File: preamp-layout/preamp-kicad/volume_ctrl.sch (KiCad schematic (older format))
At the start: 63 parts, among them J65 Conn_01x02_Male, J66 Conn_01x02_Male, J67 Conn_01x03_Female, J68 Conn_01x03_Female, J69 Conn_01x03_Male, J70 Conn_01x03_Male, J71 Conn_01x03_Male, U12 MCP4902, U13 MCP4902, U14 TL072, U15 TL072, U16 THAT2181, U17 THAT2181, U18 TL072, U19 THAT2181, U20 THAT2181, U21 TL072

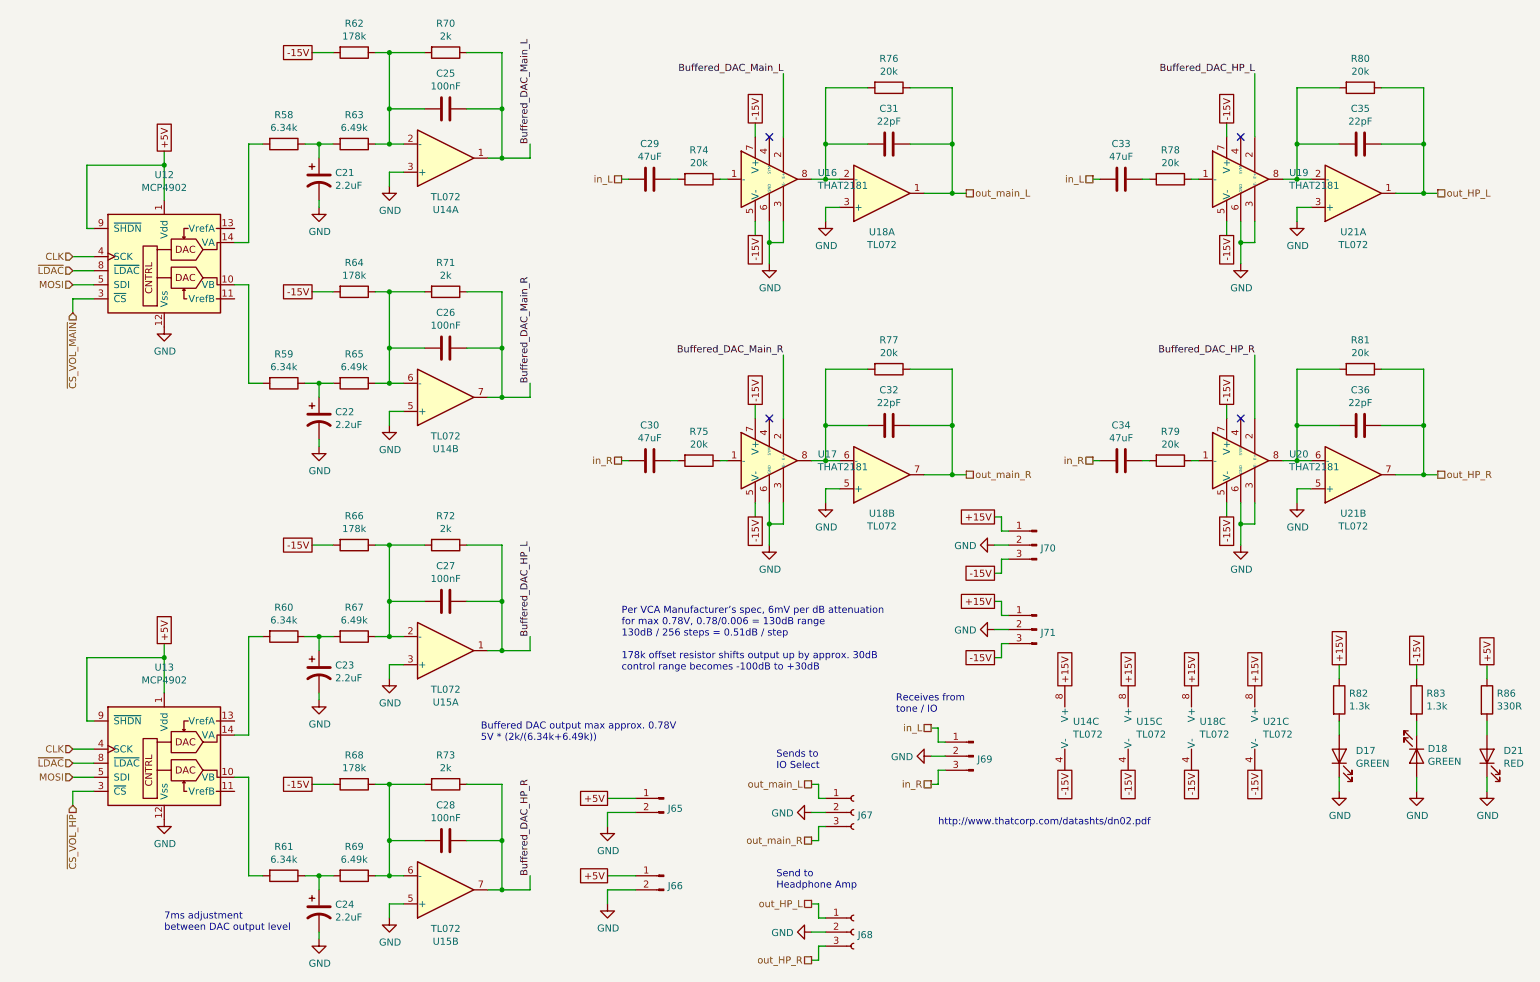
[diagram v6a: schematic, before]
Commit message: Initial Review
Reviewing schematic, comparing to references and filling in BOM to match schematics. Updating footprints in the process as well.
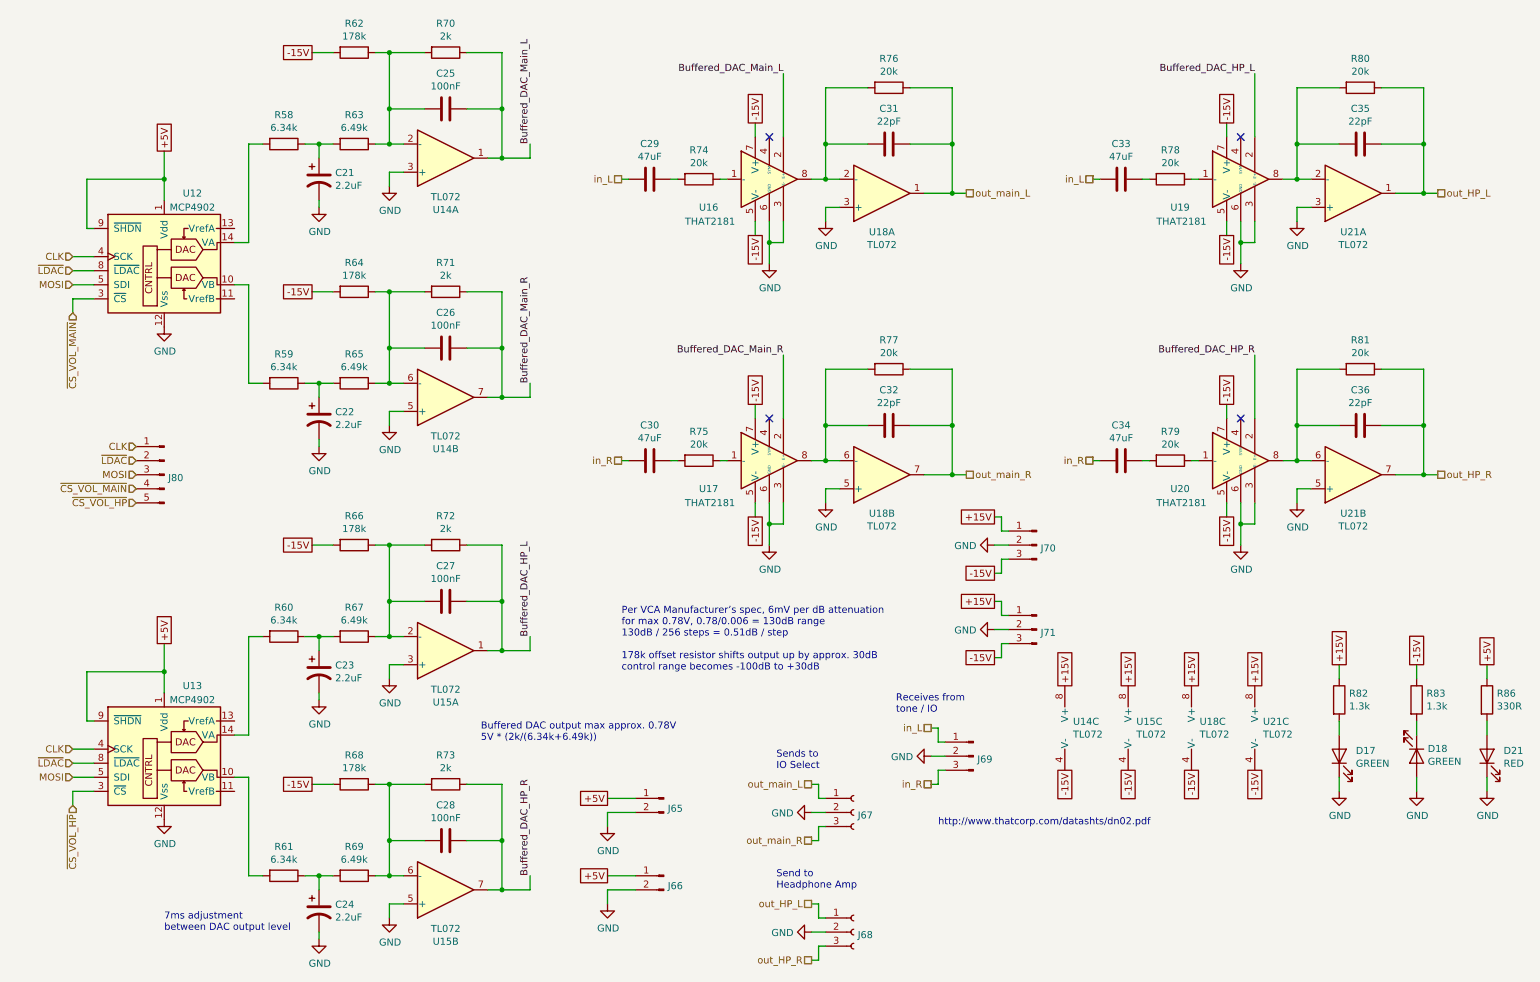
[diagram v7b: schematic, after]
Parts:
- added J80: Conn_01x05_Male, symbol Connector:Conn_01x05_Male
- C25, C26, C27, C28: footprint (none) -> Capacitor_SMD:C_0805_2012Metric_Pad1.15x1.40mm_HandSolder
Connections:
- net CLK: now also J80.1 (Pin_1)
- net MOSI: now also J80.3 (Pin_3)
- net ~CS_VOL_HP: now also J80.5 (Pin_5)
- net ~CS_VOL_MAIN: now also J80.4 (Pin_4)
- net ~LDAC: now also J80.2 (Pin_2)
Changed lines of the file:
@@
 $Descr A4 11693 8268
 encoding utf-8
-Sheet 11 12
+Sheet 12 12
 Title ""
 Date "2020-01-23"
@@
 F 0 "C25" V 3248 1400 50  0000 C CNN
 F 1 "100nF" V 3339 1400 50  0000 C CNN
-F 2 "" H 3538 1250 50  0001 C CNN
+F 2 "Capacitor_SMD:C_0805_2012Metric_Pad1.15x1.40mm_HandSolder" H 3538 1250 50  0001 C CNN
 F 3 "~" H 3500 1400 50  0001 C CNN
 	1    3500 1400
@@
 U 1 1 6017A289
 P 1500 2450
-F 0 "U12" H 1500 3031 50  0000 C CNN
-F 1 "MCP4902" H 1500 2940 50  0000 C CNN
+F 0 "U12" H 1700 2900 50  0000 C CNN
+F 1 "MCP4902" H 1700 2800 50  0000 C CNN
 F 2 "" H 2300 2150 50  0001 C CNN
 F 3 "http://ww1.microchip.com/downloads/en/DeviceDoc/22250A.pdf" H 2300 2150 50  0001 C CNN
@@
 U 1 1 6017683C
 P 5800 1900
-F 0 "U16" H 6144 1946 50  0000 L CNN
-F 1 "THAT2181" H 6144 1855 50  0000 L CNN
+F 0 "U16" H 5300 1700 50  0000 L CNN
+F 1 "THAT2181" H 5200 1600 50  0000 L CNN
 F 2 "" H 5800 1900 50  0001 C CNN
 F 3 "http://www.thatcorp.com/datashts/THAT_2181-Series_Datasheet.pdf" H 5800 1900 50  0001 C CNN
@@
 F 0 "C26" V 3248 3100 50  0000 C CNN
 F 1 "100nF" V 3339 3100 50  0000 C CNN
-F 2 "" H 3538 2950 50  0001 C CNN
+F 2 "Capacitor_SMD:C_0805_2012Metric_Pad1.15x1.40mm_HandSolder" H 3538 2950 50  0001 C CNN
 F 3 "~" H 3500 3100 50  0001 C CNN
 	1    3500 3100
@@
 U 1 1 602F6E92
 P 5800 3900
-F 0 "U17" H 6144 3946 50  0000 L CNN
-F 1 "THAT2181" H 6144 3855 50  0000 L CNN
+F 0 "U17" H 5300 3700 50  0000 L CNN
+F 1 "THAT2181" H 5200 3600 50  0000 L CNN
 F 2 "" H 5800 3900 50  0001 C CNN
 F 3 "http://www.thatcorp.com/datashts/THAT_2181-Series_Datasheet.pdf" H 5800 3900 50  0001 C CNN
@@
 F 0 "C27" V 3248 4900 50  0000 C CNN
 F 1 "100nF" V 3339 4900 50  0000 C CNN
-F 2 "" H 3538 4750 50  0001 C CNN
+F 2 "Capacitor_SMD:C_0805_2012Metric_Pad1.15x1.40mm_HandSolder" H 3538 4750 50  0001 C CNN
 F 3 "~" H 3500 4900 50  0001 C CNN
 	1    3500 4900
@@
 U 1 1 6033B91D
 P 1500 5950
-F 0 "U13" H 1500 6531 50  0000 C CNN
-F 1 "MCP4902" H 1500 6440 50  0000 C CNN
+F 0 "U13" H 1700 6400 50  0000 C CNN
+F 1 "MCP4902" H 1700 6300 50  0000 C CNN
 F 2 "" H 2300 5650 50  0001 C CNN
 F 3 "http://ww1.microchip.com/downloads/en/DeviceDoc/22250A.pdf" H 2300 5650 50  0001 C CNN
@@
 U 1 1 6033B96D
 P 9150 1900
-F 0 "U19" H 9494 1946 50  0000 L CNN
-F 1 "THAT2181" H 9494 1855 50  0000 L CNN
+F 0 "U19" H 8650 1700 50  0000 L CNN
+F 1 "THAT2181" H 8550 1600 50  0000 L CNN
 F 2 "" H 9150 1900 50  0001 C CNN
 F 3 "http://www.thatcorp.com/datashts/THAT_2181-Series_Datasheet.pdf" H 9150 1900 50  0001 C CNN
@@
 F 0 "C28" V 3248 6600 50  0000 C CNN
 F 1 "100nF" V 3339 6600 50  0000 C CNN
-F 2 "" H 3538 6450 50  0001 C CNN
+F 2 "Capacitor_SMD:C_0805_2012Metric_Pad1.15x1.40mm_HandSolder" H 3538 6450 50  0001 C CNN
 F 3 "~" H 3500 6600 50  0001 C CNN
 	1    3500 6600
@@
 U 1 1 6033BA78
 P 9150 3900
-F 0 "U20" H 9494 3946 50  0000 L CNN
-F 1 "THAT2181" H 9494 3855 50  0000 L CNN
+F 0 "U20" H 8650 3700 50  0000 L CNN
+F 1 "THAT2181" H 8550 3600 50  0000 L CNN
 F 2 "" H 9150 3900 50  0001 C CNN
 F 3 "http://www.thatcorp.com/datashts/THAT_2181-Series_Datasheet.pdf" H 9150 3900 50  0001 C CNN
@@
 	850  2550 1000 2550
 Wire Wire Line
-	1500 1700 1500 1800
-Wire Wire Line
 	1000 2250 950  2250
 Wire Wire Line
-	950  2250 950  1800
-Connection ~ 1500 1800
-Wire Wire Line
-	1500 1800 1500 2050
+	950  2250 950  1900
 Wire Wire Line
 	1000 5750 950  5750
 Wire Wire Line
-	950  5750 950  5300
-Wire Wire Line
-	950  5300 1500 5300
+	950  5750 950  5400
+Wire Wire Line
+	950  5400 1500 5400
 Text GLabel 1500 5200 1    50   UnSpc ~ 0
 +5V
 Wire Wire Line
-	1500 5200 1500 5300
-Wire Wire Line
-	1500 5300 1500 5550
-Connection ~ 1500 5300
-Wire Wire Line
-	950  1800 1500 1800
+	950  1900 1500 1900
 Text GLabel 1500 1700 1    50   UnSpc ~ 0
 +5V
@@
 	-1   0    0    -1
 $EndComp
+Connection ~ 1500 1900
+Wire Wire Line
+	1500 1900 1500 2050
+Wire Wire Line
+	1500 1700 1500 1900
+Connection ~ 1500 5400
+Wire Wire Line
+	1500 5400 1500 5550
+Wire Wire Line
+	1500 5200 1500 5400
+$Comp
+L Connector:Conn_01x05_Male J80
+U 1 1 5F064263
+P 1500 4000
+F 0 "J80" H 1472 3978 50  0000 R CNN
+F 1 "Conn_01x05_Male" H 1608 4290 50  0001 C CNN
+F 2 "" H 1500 4000 50  0001 C CNN
+F 3 "~" H 1500 4000 50  0001 C CNN
+	1    1500 4000
+	-1   0    0    -1
+$EndComp
+Text HLabel 1300 4000 0    50   Input ~ 0
+MOSI
+Text HLabel 1300 3800 0    50   Input ~ 0
+CLK
+Text HLabel 1300 3900 0    50   Input ~ 0
+~LDAC
+Text HLabel 1300 4100 0    50   Input ~ 0
+~CS_VOL_MAIN
+Text HLabel 1300 4200 0    50   Input ~ 0
+~CS_VOL_HP
 $EndSCHEMATC
